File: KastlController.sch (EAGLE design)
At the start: 17 parts

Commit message: Update KastlController.sch
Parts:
- removed GESTUREBOARD: GESTUREBOARD_INTERFACE, gestureBoardInterface_Kastl:GESTUREBOARD_INTERFACE
- removed GESTUREBOARD_PWR: GESTUREBOARD_POWER, gestureBoardInterface_Kastl:GESTUREBOARD_POWER
- removed GND_PSU, VCC12: (no value), wirepad:2,54/1,0
- removed J_BT_BOARD_1: BLUETOOTH_BOARDSTANDING, Bluetooth_HC-06:BLUETOOTH_BOARDSTANDING
- removed PW_REG_3_3V: STEPDOWN_5V-3_3V, 5V3_3V_stepdown:STEPDOWN_5V-3_3V
- added 12V_PSU: PWR_CONNECTOR, PowerConnector:PWR_CONNECTOR
- added 5V_3V3_CONV: STEPDOWN_5V-3_3V, 5V3_3V_stepdown:STEPDOWN_5V-3_3V
- added C5: (no value), htl3r-discrete:C-EU_025-024X044
- added GESTURE_POWER: GESTUREBOARD_POWER, gestureBoardInterface_Kastl:GESTUREBOARD_POWER
- added HC-06_BLUETOOTH: BLUETOOTH_BOARDSTANDING, Bluetooth_HC-06:BLUETOOTH_BOARDSTANDING
- added LED1: (no value), htl3r-discrete:LEDS_5MM
- added R1: 100k, htl3r-discrete:R-EU_0204/2V
- added R2: 220k, htl3r-discrete:R-EU_0204/2V
- added R3: 10k, htl3r-discrete:R-EU_0204/2V
- added R4: 2k2, htl3r-discrete:R-EU_0204/2V
- added REAL_TIME_CLOCK: DS3231_RTC_MODULE, DS3231_RTC:DS3231_RTC_MODULE
- added Y1: 32.768kHz, SparkFun-FreqCtrl:CRYSTAL3.2X1.5MM
- U$1: value 3_3/5V_LEVELCONVERTER -> GESTUREBOARD; device LogicLevelConv_Kastl:3_3/5V_LEVELCONVERTER -> gestureBoardInterface_Kastl:GESTUREBOARD
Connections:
- removed net VCC12: LEDSTRIP_DRW.VCC12, LEDSTRIP_MID.VCC12, LEDSTRIP_TOP.VCC12, VCC12.P
- removed net VCC5: ATMEGA328P.VCC, C1.1, C2.1, C3.1, C4.1, J_BT_BOARD_1.VCC, MOBILE_OUT.VBUS, PW_REG_3_3V.VIN, PW_REG_5V.VBUS, U$1.VCC5
- new net +12V: 12V_PSU.VOUT, LEDSTRIP_DRW.VCC12, LEDSTRIP_MID.VCC12, LEDSTRIP_TOP.VCC12
- new net +3V3: 5V_3V3_CONV.VOUT, C1.1, C2.1, GESTURE_POWER.VCC3_3, HC-06_BLUETOOTH.VCC, U$1.VCC_3V3
- new net +5V: 5V_3V3_CONV.VIN, ATMEGA328P.AREF, ATMEGA328P.AVCC, ATMEGA328P.VCC, C3.1, C4.1, C5.1, MOBILE_OUT.VBUS, PW_REG_5V.VBUS, R3.2, REAL_TIME_CLOCK.VCC
- new net N$13: ATMEGA328P.PC4(ADC4/SDA), REAL_TIME_CLOCK.SDA
- new net N$15: ATMEGA328P.PC5(ADC5/SCL), REAL_TIME_CLOCK.SCL
- new net N$16: HC-06_BLUETOOTH.RX, R1.1, R2.2
- net GND: now also 12V_PSU.GND, 5V_3V3_CONV.GND, ATMEGA328P.GND@1, C5.2, GESTURE_POWER.GND, HC-06_BLUETOOTH.GND, LED1.C, R2.1, REAL_TIME_CLOCK.GND, Y1.2; no longer GESTUREBOARD_PWR.GND, GND_PSU.P, J_BT_BOARD_1.GND, PW_REG_3_3V.GND
- net N$10: now also LED1.A, R4.1; no longer ATMEGA328P.PD1(TXD), U$1.RXI_CH1
- net N$11: now also REAL_TIME_CLOCK.OSC, Y1.1; no longer J_BT_BOARD_1.TX, U$1.TXI_CH1
- net N$12: now also ATMEGA328P.PC6(/RESET), R3.1; no longer J_BT_BOARD_1.RX, U$1.RXO_CH1
- net N$14: now also ATMEGA328P.PD0(RXD), HC-06_BLUETOOTH.TX; no longer GESTUREBOARD_PWR.VCC3_3, PW_REG_3_3V.VOUT, U$1.VCC3_3
- net N$3: now also U$1.GPIN1; no longer GESTUREBOARD.GPIN1
- net N$4: now also U$1.GPIN2; no longer GESTUREBOARD.GPIN2
- net N$5: now also U$1.GPIN3; no longer GESTUREBOARD.GPIN3
- net N$6: now also U$1.GPIN6; no longer GESTUREBOARD.GPIN6
- net N$7: now also U$1.GPIN7; no longer GESTUREBOARD.GPIN7
- net N$9: now also ATMEGA328P.PD1(TXD), R1.2; no longer ATMEGA328P.PD0(RXD), U$1.TXO_CH1
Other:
- moved on the sheet: C1, C2, C3, C4, MOBILE_OUT, PW_REG_5V

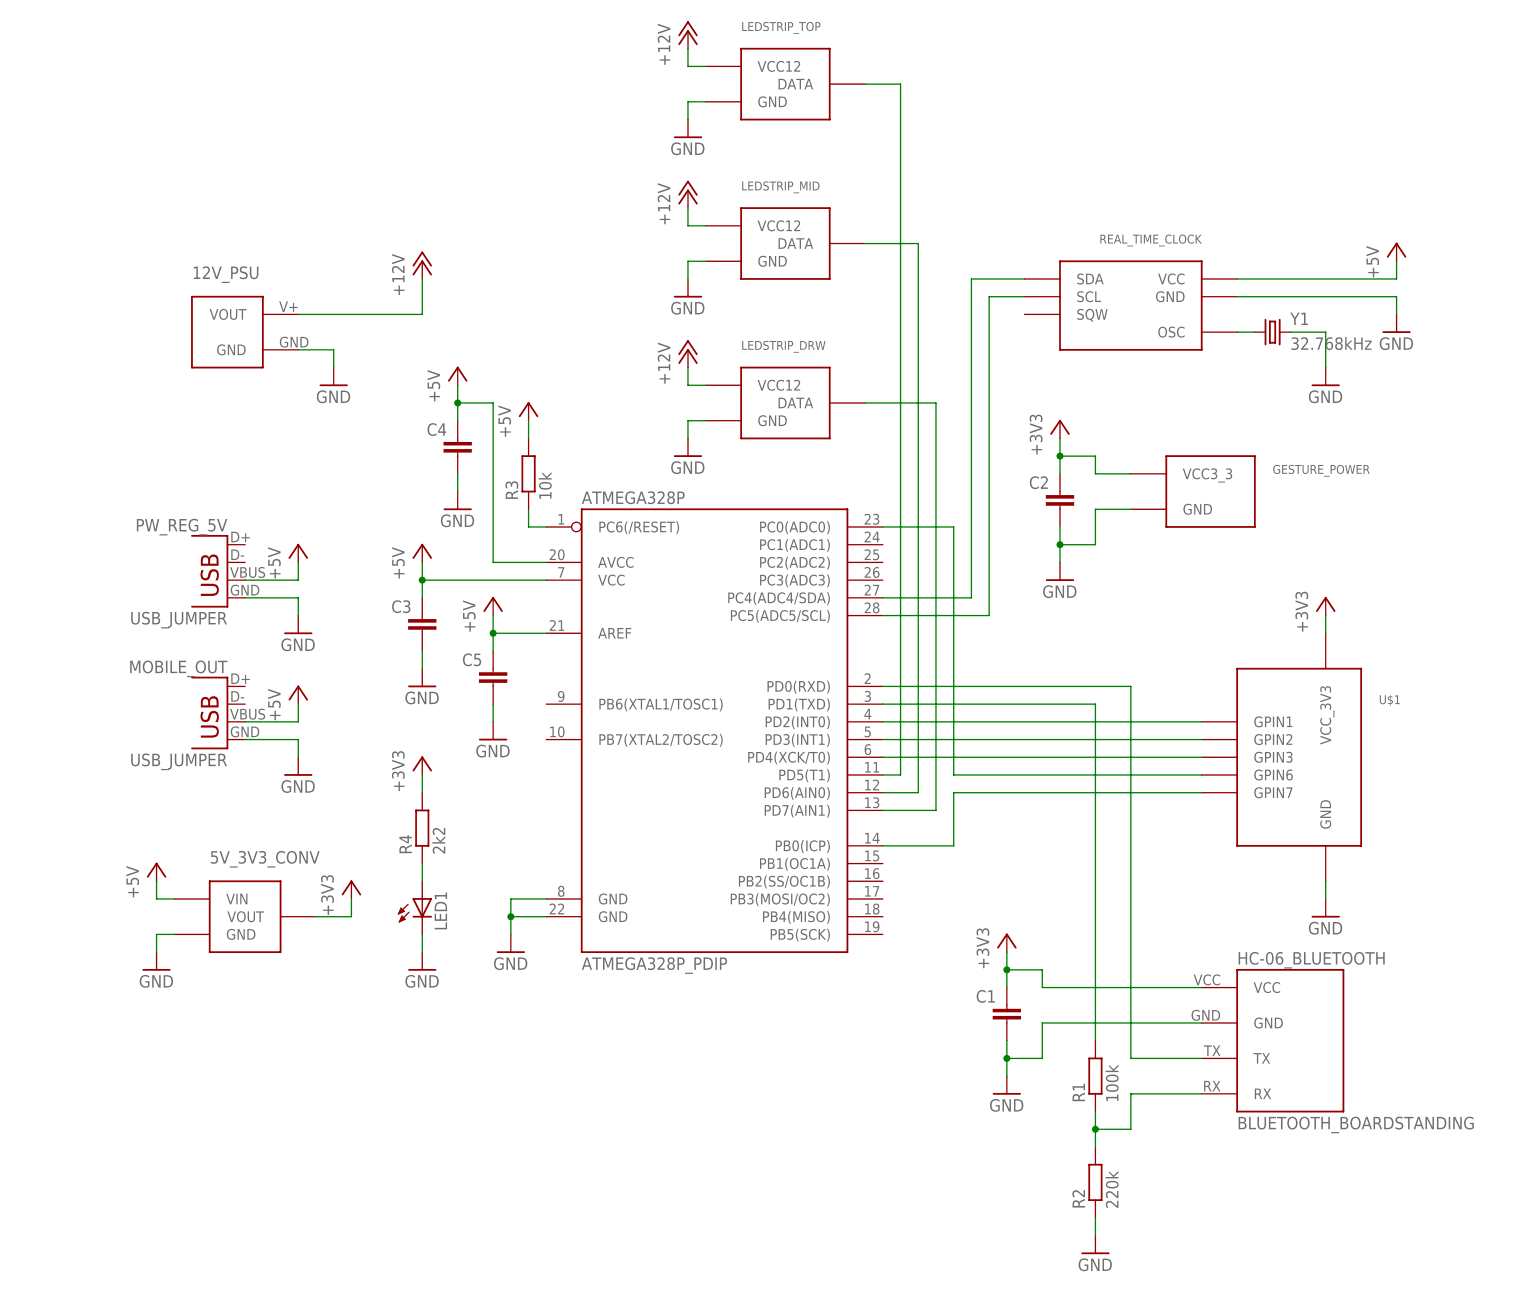
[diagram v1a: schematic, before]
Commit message: changed voltage regulators, cleanup
added voltage regulator libraries and changed some minor things
corrected a mistake with the oscillator of the real time clock module
(no oscillator is needed since it is already integrated)
updated readme
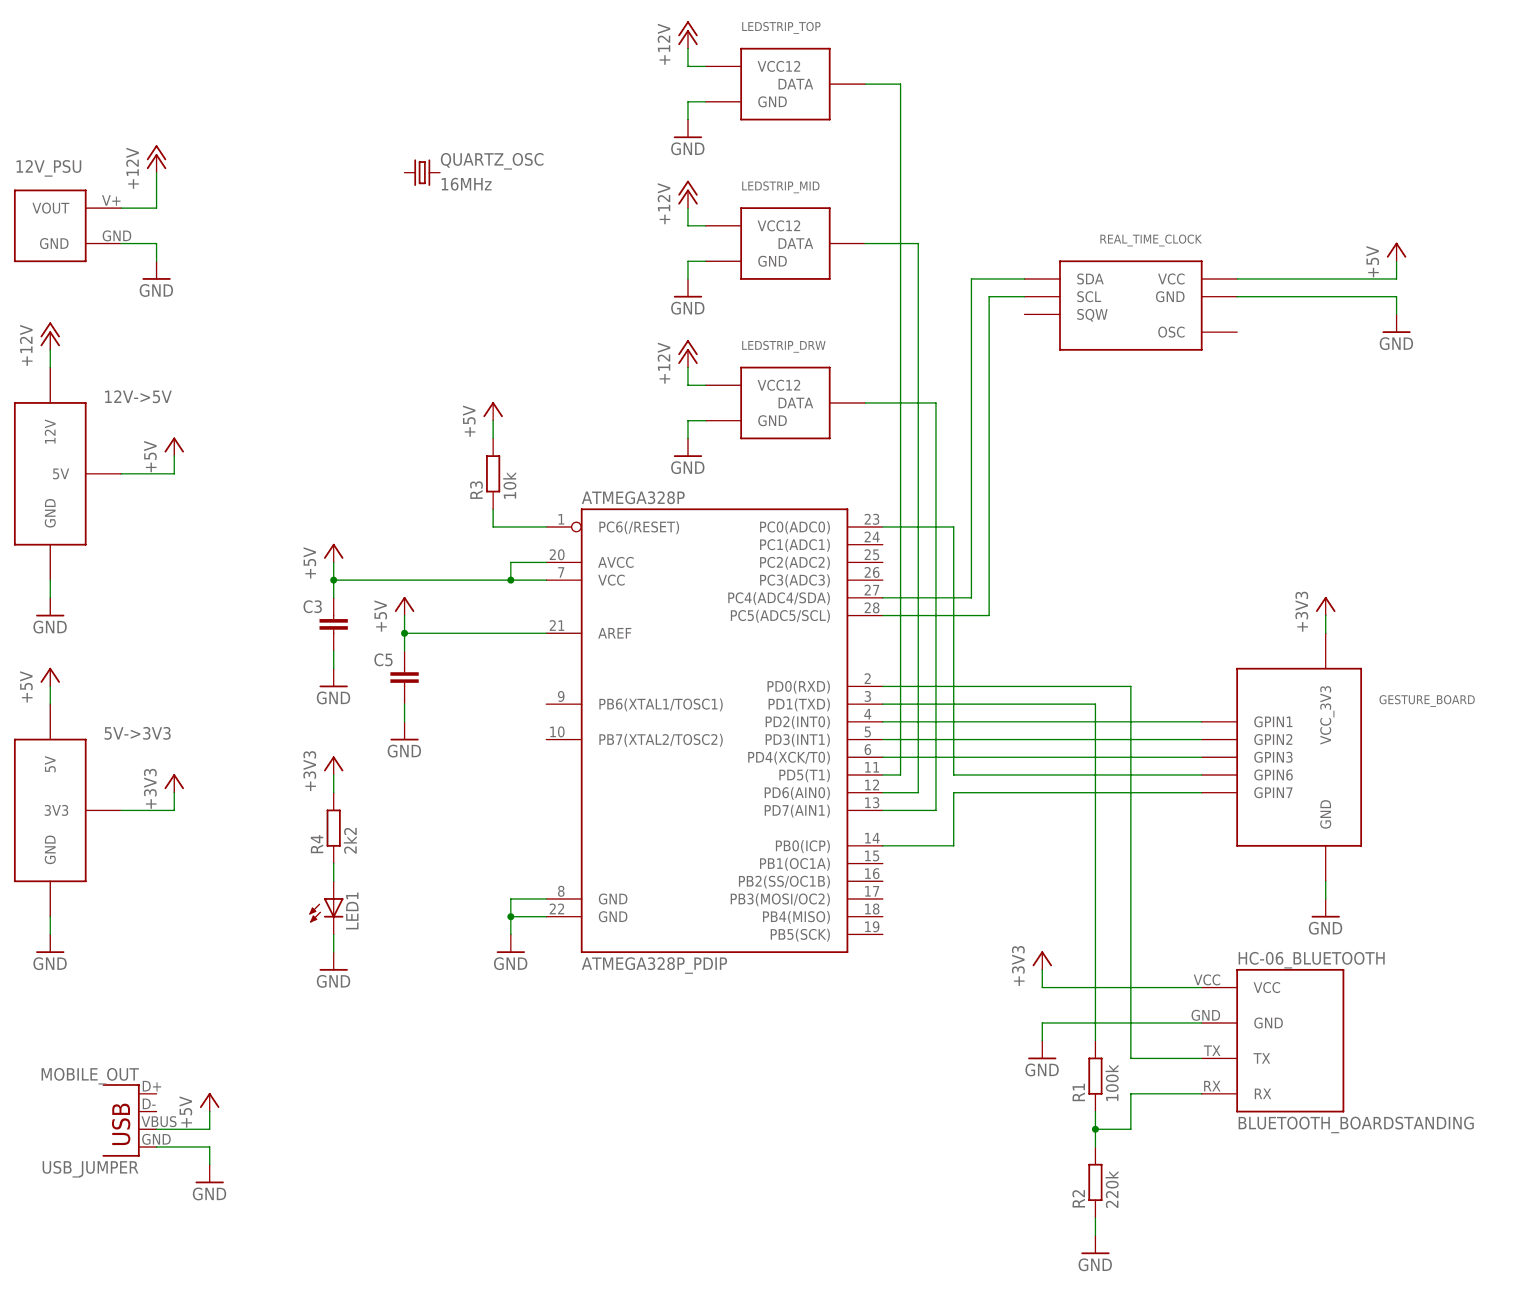
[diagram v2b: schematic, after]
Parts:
- removed 5V_3V3_CONV: STEPDOWN_5V-3_3V, 5V3_3V_stepdown:STEPDOWN_5V-3_3V
- removed C1, C2, C4: (no value), htl3r-discrete:C-EU_025-024X044
- removed GESTURE_POWER: GESTUREBOARD_POWER, gestureBoardInterface_Kastl:GESTUREBOARD_POWER
- removed PW_REG_5V: USB_JUMPER, SparkFun-Connectors:USB_JUMPER
- removed Y1: 32.768kHz, SparkFun-FreqCtrl:CRYSTAL3.2X1.5MM
- added 12V->5V: VOLTAGE_REG_12V_5V, Voltage_Regulators:VOLTAGE_REG_12V_5V
- added 5V->3V3: VOLTAGE_REG_5V_3V3, Voltage_Regulators:VOLTAGE_REG_5V_3V3
- added QUARTZ_OSC: 16MHz, crystal:CRYSTALHC33U-V
- renumbered U$1 to GESTURE_BOARD
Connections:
- removed net N$11: REAL_TIME_CLOCK.OSC, Y1.1
- net +12V: now also 12V->5V.12V
- net +3V3: now also 5V->3V3.3V3, R4.2; no longer 5V_3V3_CONV.VOUT, C1.1, C2.1, GESTURE_POWER.VCC3_3
- net +5V: now also 12V->5V.5V, 5V->3V3.5V; no longer 5V_3V3_CONV.VIN, C4.1, PW_REG_5V.VBUS
- net GND: now also 12V->5V.GND, 5V->3V3.GND; no longer 5V_3V3_CONV.GND, C1.2, C2.2, C4.2, GESTURE_POWER.GND, PW_REG_5V.GND, Y1.2
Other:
- moved on the sheet: 12V_PSU, C3, C5, LED1, MOBILE_OUT, R3, R4
